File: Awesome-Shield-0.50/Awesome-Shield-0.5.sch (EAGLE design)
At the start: 37 parts, among them J2 ARDUINO_R3_SHIELD, SW1 SPST_TACT-EVQQ2, U1 LIGHTSENSORTEMT6000

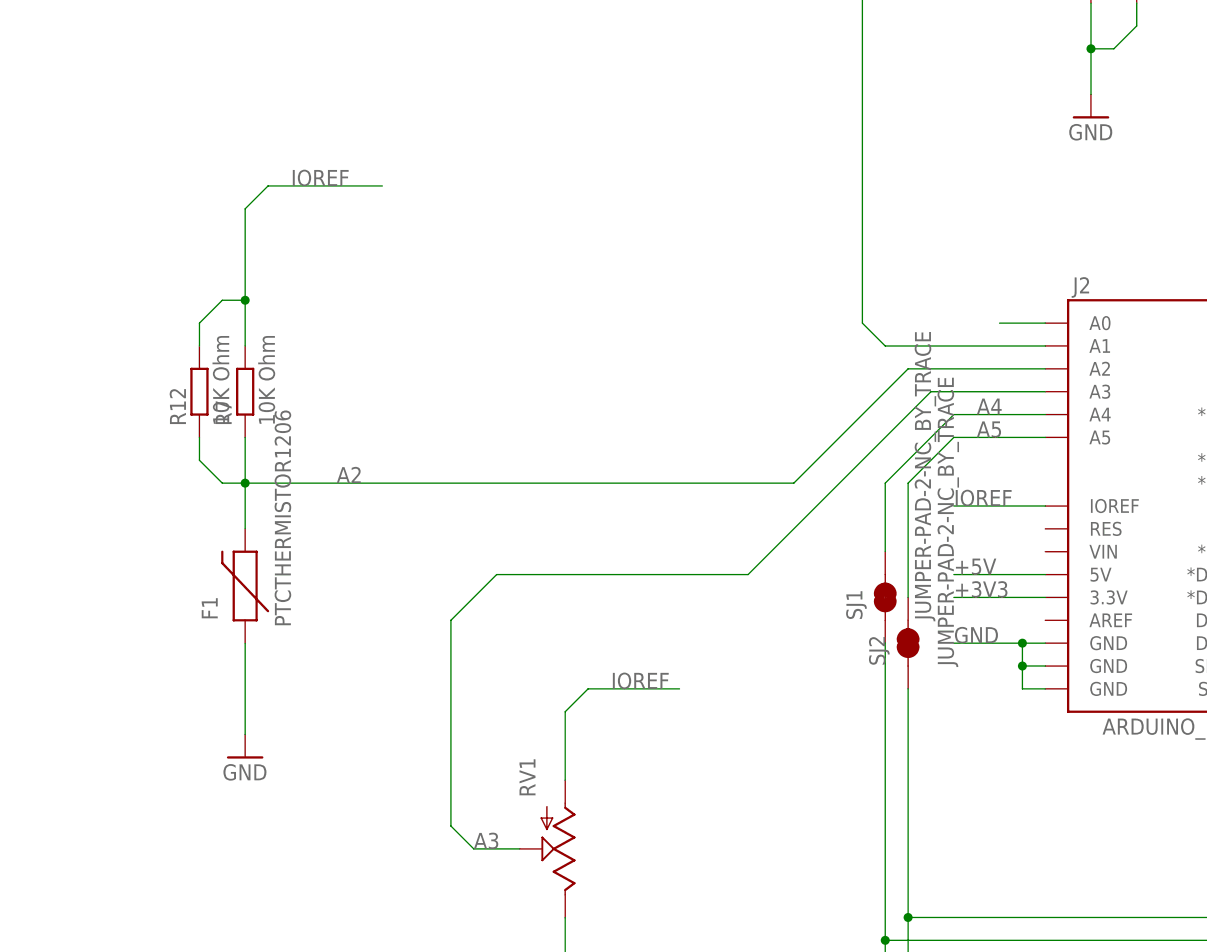
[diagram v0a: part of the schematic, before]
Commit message: rm thermistor
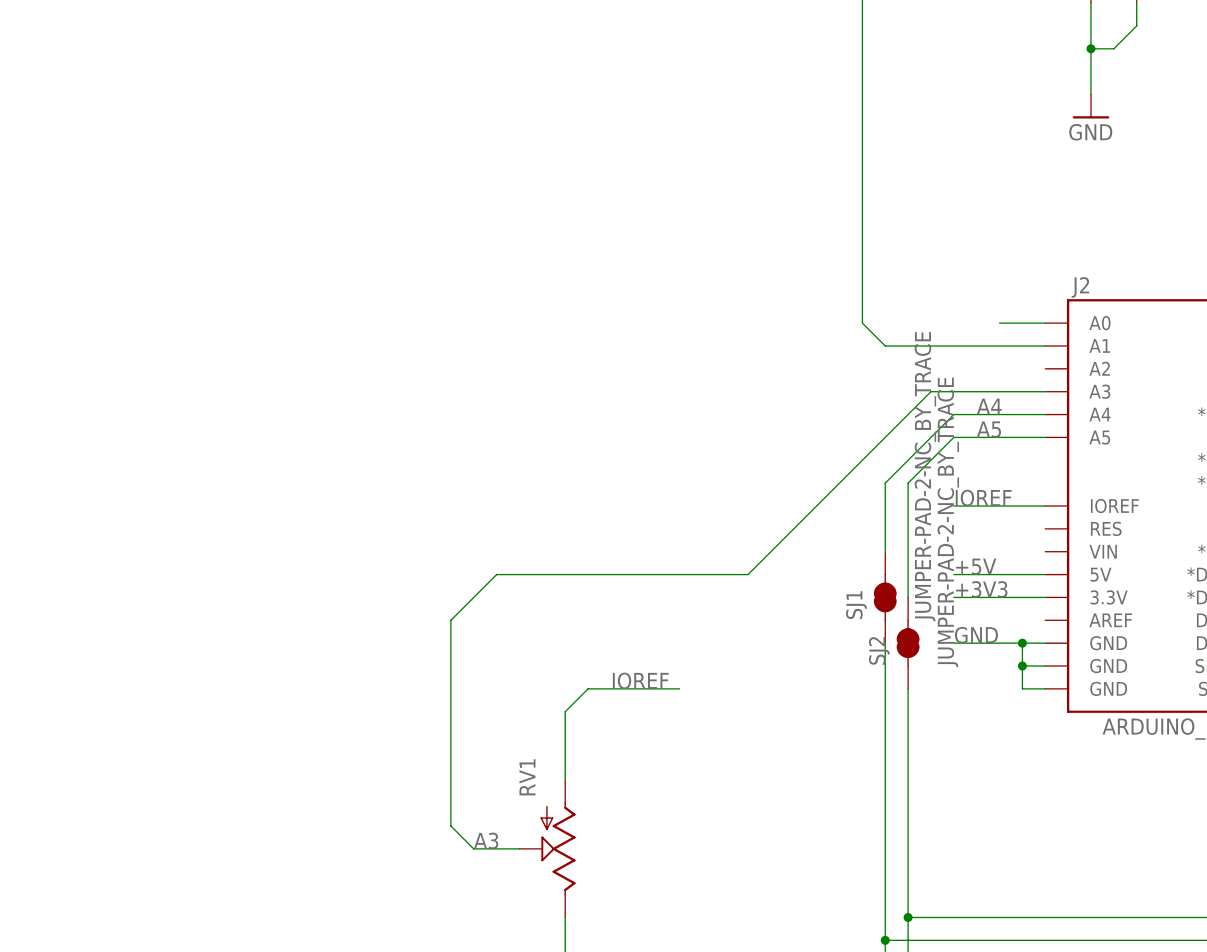
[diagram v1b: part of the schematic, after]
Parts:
- removed F1: PTCTHERMISTOR1206, SparkFun-PowerIC:PTCTHERMISTOR1206
- removed R12: 10K Ohm, rcl:R-EU_R0603
- removed R7: 10K Ohm, rcl:R-EU_R1206
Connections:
- removed net A2: F1.2, J2.A2, R12.1, R7.1
- net GND: no longer F1.1
- net IOREF: no longer R12.2, R7.2
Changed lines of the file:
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@@
 <part name="R3" library="rcl" deviceset="R-EU_" device="R1206" value="130 Ohm"/>
 <part name="R6" library="rcl" deviceset="R-EU_" device="R1206" value="10K"/>
-<part name="R7" library="rcl" deviceset="R-EU_" device="R1206" value="10K Ohm"/>
-<part name="F1" library="SparkFun-PowerIC" deviceset="PTC" device="THERMISTOR1206"/>
 <part name="SW1" library="adafruit" deviceset="SPST_TACT" device="-EVQQ2"/>
 <part name="GND1" library="supply1" deviceset="GND" device=""/>
 <part name="GND2" library="supply1" deviceset="GND" device=""/>
-<part name="GND3" library="supply1" deviceset="GND" device=""/>
 <part name="GND4" library="supply1" deviceset="GND" device=""/>
 <part name="GND5" library="supply1" deviceset="GND" device=""/>
@@
 <part name="R10" library="rcl" deviceset="R-EU_" device="R0603" value="130 Ohm"/>
 <part name="R11" library="rcl" deviceset="R-EU_" device="R0603" value="10K"/>
-<part name="R12" library="rcl" deviceset="R-EU_" device="R0603" value="10K Ohm"/>
 <part name="J3" library="Seeed-OPL-Connector" deviceset="GROVE-CONNECTOR-SMD(4+2P-2.0)" device=""/>
 <part name="J4" library="Seeed-OPL-Connector" deviceset="GROVE-CONNECTOR-SMD(4+2P-2.0)" device=""/>
@@
 <instance part="R3" gate="G$1" x="274.32" y="134.62"/>
 <instance part="R6" gate="G$1" x="187.96" y="190.5" rot="R270"/>
-<instance part="R7" gate="G$1" x="93.98" y="142.24" rot="R90"/>
-<instance part="F1" gate="G$1" x="93.98" y="119.38" rot="R90"/>
 <instance part="SW1" gate="G$1" x="269.24" y="210.82"/>
 <instance part="GND1" gate="1" x="307.34" y="127"/>
 <instance part="GND2" gate="1" x="187.96" y="172.72"/>
-<instance part="GND3" gate="1" x="93.98" y="101.6"/>
 <instance part="GND4" gate="1" x="129.54" y="68.58"/>
 <instance part="GND5" gate="1" x="269.24" y="190.5"/>
@@
 <instance part="R10" gate="G$1" x="254" y="129.54"/>
 <instance part="R11" gate="G$1" x="193.04" y="190.5" rot="R90"/>
-<instance part="R12" gate="G$1" x="88.9" y="142.24" rot="R90"/>
 <instance part="J3" gate="G$1" x="180.34" y="57.15"/>
 <instance part="J4" gate="G$1" x="337.82" y="64.77"/>
@@
 <net name="GND" class="0">
 <segment>
-<pinref part="F1" gate="G$1" pin="1"/>
-<pinref part="GND3" gate="1" pin="GND"/>
-<wire x1="93.98" y1="114.3" x2="93.98" y2="104.14" width="0.1524" layer="91"/>
-</segment>
-<segment>
 <pinref part="LED1" gate="G$1" pin="BLUE_C"/>
 <wire x1="299.72" y1="144.78" x2="304.8" y2="144.78" width="0.1524" layer="91"/>
@@
 <wire x1="187.96" y1="175.26" x2="187.96" y2="180.34" width="0.1524" layer="91"/>
 <junction x="187.96" y="180.34"/>
-</segment>
-</net>
-<net name="A2" class="0">
-<segment>
-<pinref part="R7" gate="G$1" pin="1"/>
-<pinref part="F1" gate="G$1" pin="2"/>
-<wire x1="93.98" y1="137.16" x2="93.98" y2="132.08" width="0.1524" layer="91"/>
-<wire x1="93.98" y1="132.08" x2="93.98" y2="127" width="0.1524" layer="91"/>
-<wire x1="93.98" y1="132.08" x2="154.94" y2="132.08" width="0.1524" layer="91"/>
-<wire x1="154.94" y1="132.08" x2="167.64" y2="144.78" width="0.1524" layer="91"/>
-<junction x="93.98" y="132.08"/>
-<wire x1="167.64" y1="144.78" x2="182.88" y2="144.78" width="0.1524" layer="91"/>
-<wire x1="93.98" y1="132.08" x2="91.44" y2="132.08" width="0.1524" layer="91"/>
-<wire x1="91.44" y1="132.08" x2="88.9" y2="134.62" width="0.1524" layer="91"/>
-<pinref part="R12" gate="G$1" pin="1"/>
-<wire x1="88.9" y1="134.62" x2="88.9" y2="137.16" width="0.1524" layer="91"/>
-<label x="104.14" y="132.08" size="1.778" layer="95"/>
-<pinref part="J2" gate="G$1" pin="A2"/>
 </segment>
 </net>
@@
 <net name="IOREF" class="0">
 <segment>
-<pinref part="R7" gate="G$1" pin="2"/>
-<pinref part="R12" gate="G$1" pin="2"/>
-<wire x1="93.98" y1="152.4" x2="93.98" y2="147.32" width="0.1524" layer="91"/>
-<wire x1="88.9" y1="147.32" x2="88.9" y2="149.86" width="0.1524" layer="91"/>
-<wire x1="88.9" y1="149.86" x2="91.44" y2="152.4" width="0.1524" layer="91"/>
-<wire x1="91.44" y1="152.4" x2="93.98" y2="152.4" width="0.1524" layer="91"/>
-<junction x="93.98" y="152.4"/>
-<wire x1="93.98" y1="152.4" x2="93.98" y2="162.56" width="0.1524" layer="91"/>
-<wire x1="93.98" y1="162.56" x2="96.52" y2="165.1" width="0.1524" layer="91"/>
-<wire x1="96.52" y1="165.1" x2="109.22" y2="165.1" width="0.1524" layer="91"/>
-<label x="99.06" y="165.1" size="1.778" layer="95"/>
-</segment>
-<segment>
 <pinref part="RV1" gate="G$1" pin="A"/>

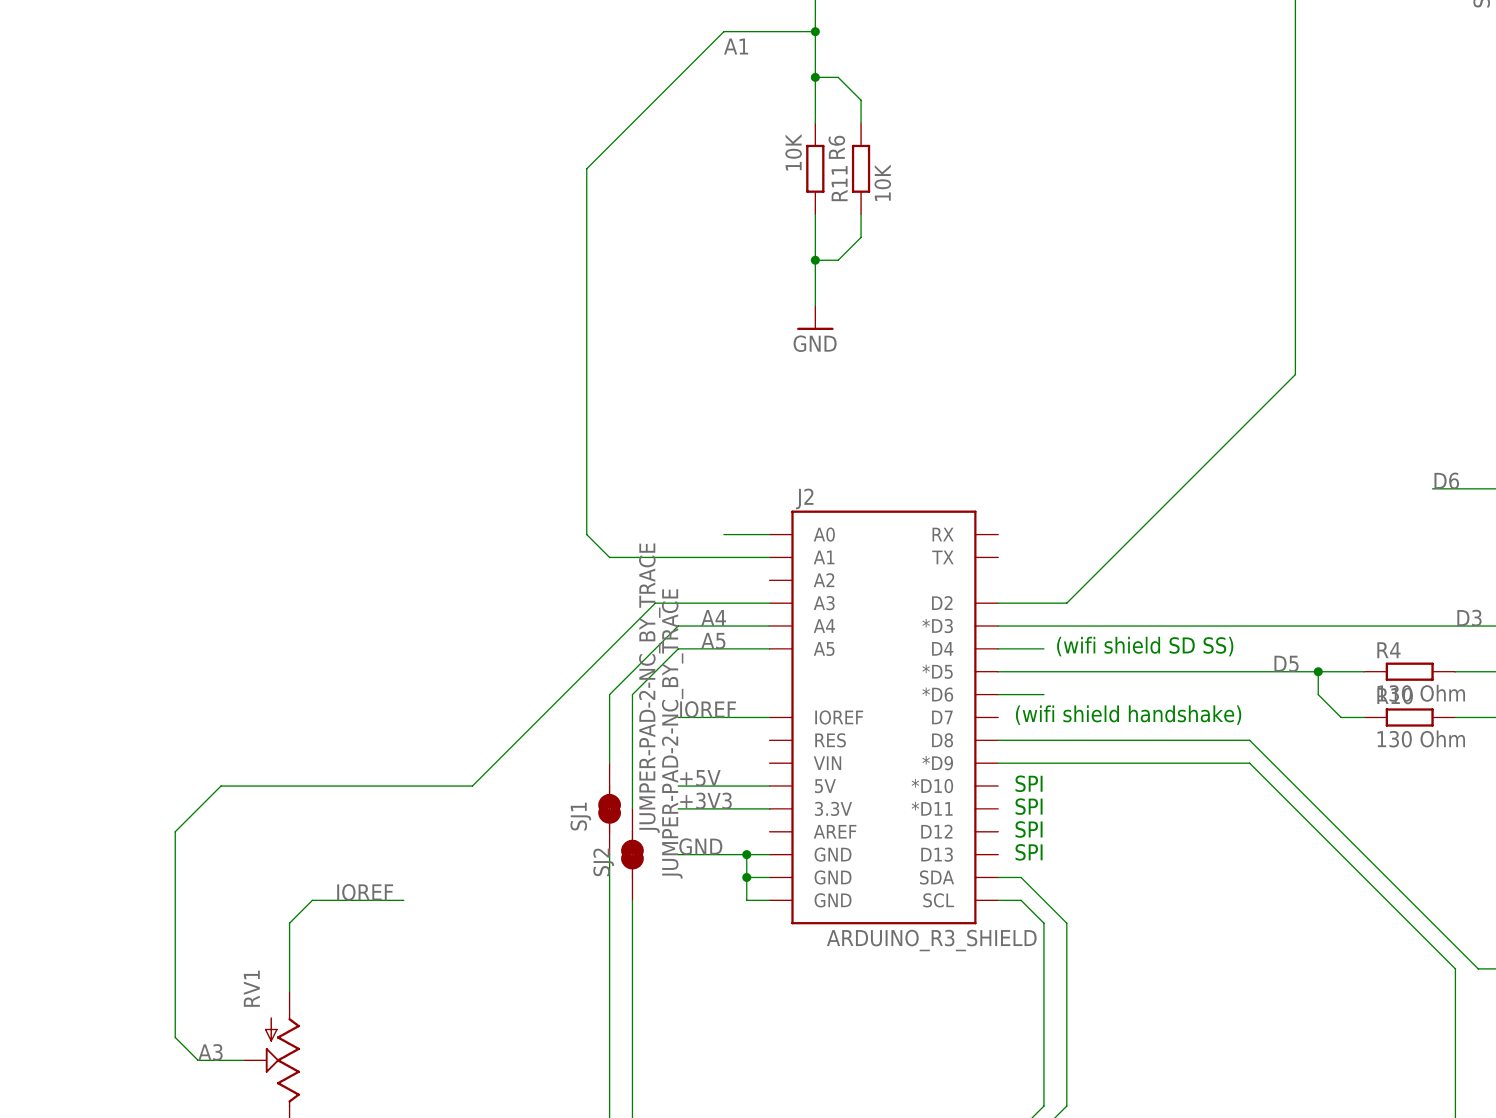
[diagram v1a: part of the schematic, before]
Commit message: swapped out shield part for headers
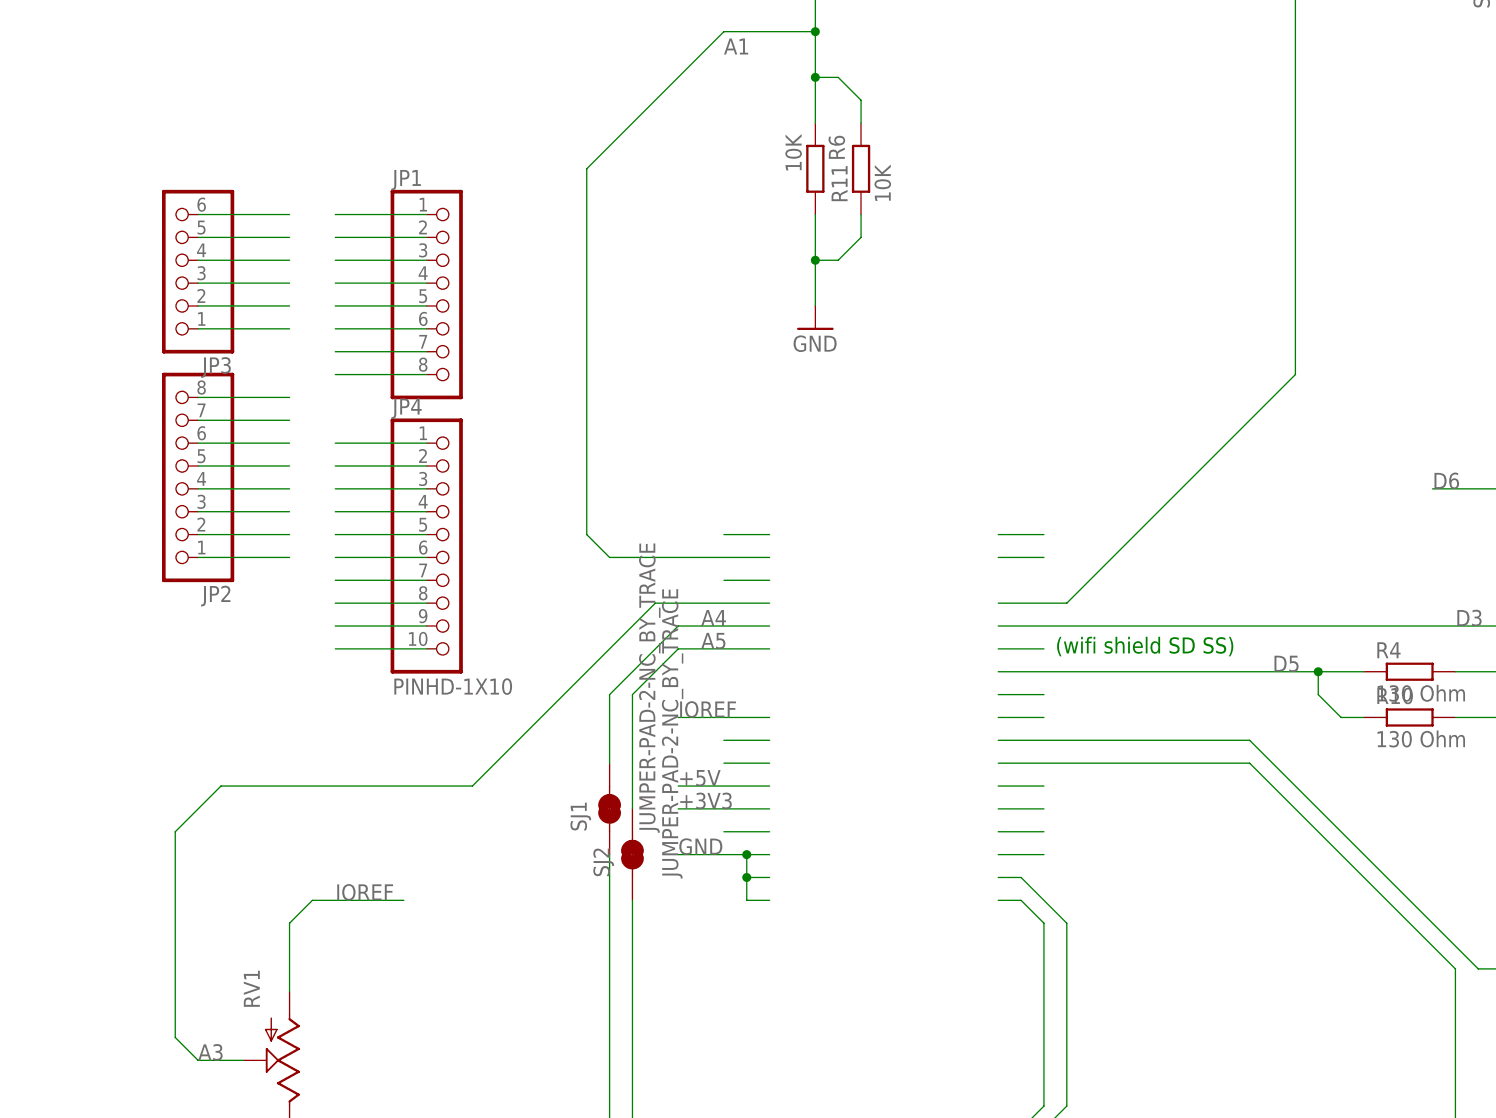
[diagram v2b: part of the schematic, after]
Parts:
- removed J2: ARDUINO_R3_SHIELD, SparkFun-Boards:ARDUINO_R3_SHIELD
- added JP1, JP2: (no value), adafruit:PINHD-1X8CLEANBIG
- added JP3: (no value), adafruit:PINHD-1X6CLEAN
- added JP4: PINHD-1X10, adafruit:PINHD-1X10
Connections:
- new net A2: JP3.3
- new net AREF: JP4.8
- new net D10: JP4.3
- new net D11: JP4.4
- new net D12: JP4.5
- new net D13: JP4.6
- new net D7: JP1.8
- new net N$39: JP2.1
- new net RES: JP2.3
- new net RX: JP1.1
- new net TX: JP1.2
- new net VIN: JP2.8
- net +3V3: now also JP2.4; no longer J2.3.3V
- net +5V: now also JP2.5; no longer J2.5V
- net A0: now also JP3.1; no longer J2.A0
- net A1: now also JP3.2; no longer J2.A1
- net A3: now also JP3.4; no longer J2.A3
- net A4: now also JP3.5; no longer J2.A4
- net A5: now also JP3.6; no longer J2.A5
- net D2: now also JP1.3; no longer J2.D2
- net D3: now also JP1.4; no longer J2.*D3
- net D4: now also JP1.5; no longer J2.D4
- net D5: now also JP1.6; no longer J2.*D5
- net D6: now also JP1.7; no longer J2.*D6
- net D8: now also JP4.1; no longer J2.D8
- net D9: now also JP4.2; no longer J2.*D9
- net GND: now also JP2.6, JP2.7, JP4.7; no longer J2.GND@0, J2.GND@1, J2.GND@2
- net IOREF: now also JP2.2; no longer J2.IOREF
- net SCL: now also JP4.10; no longer J2.SCL
- net SDA: now also JP4.9; no longer J2.SDA
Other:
- note removed: "(wifi shield handshake)"
- note removed: "SPI"
